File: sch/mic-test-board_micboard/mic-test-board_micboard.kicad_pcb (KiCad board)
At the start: 2 copper layers, 25 x 25 mm, 25 parts, among them J1 Conn_01x01, J2 Conn_01x01, J3 Conn_01x01, J4 Conn_01x01, J5 Conn_01x01, J6 Conn_01x04, U1 ICS-40730, U2 THS4531AIRUNR

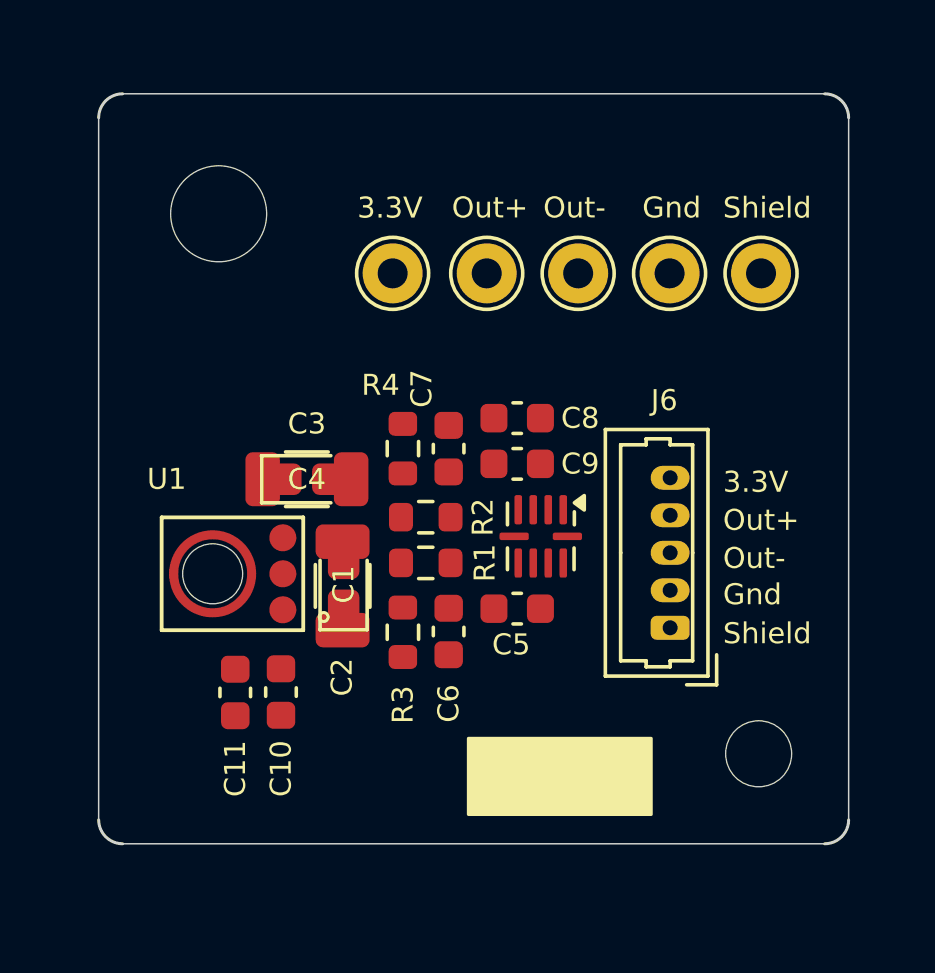
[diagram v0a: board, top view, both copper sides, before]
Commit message: pcb: finished routing mic board and ADC board.
 - BOM complete
 - uController pinout configured with CubeMX and re-checked
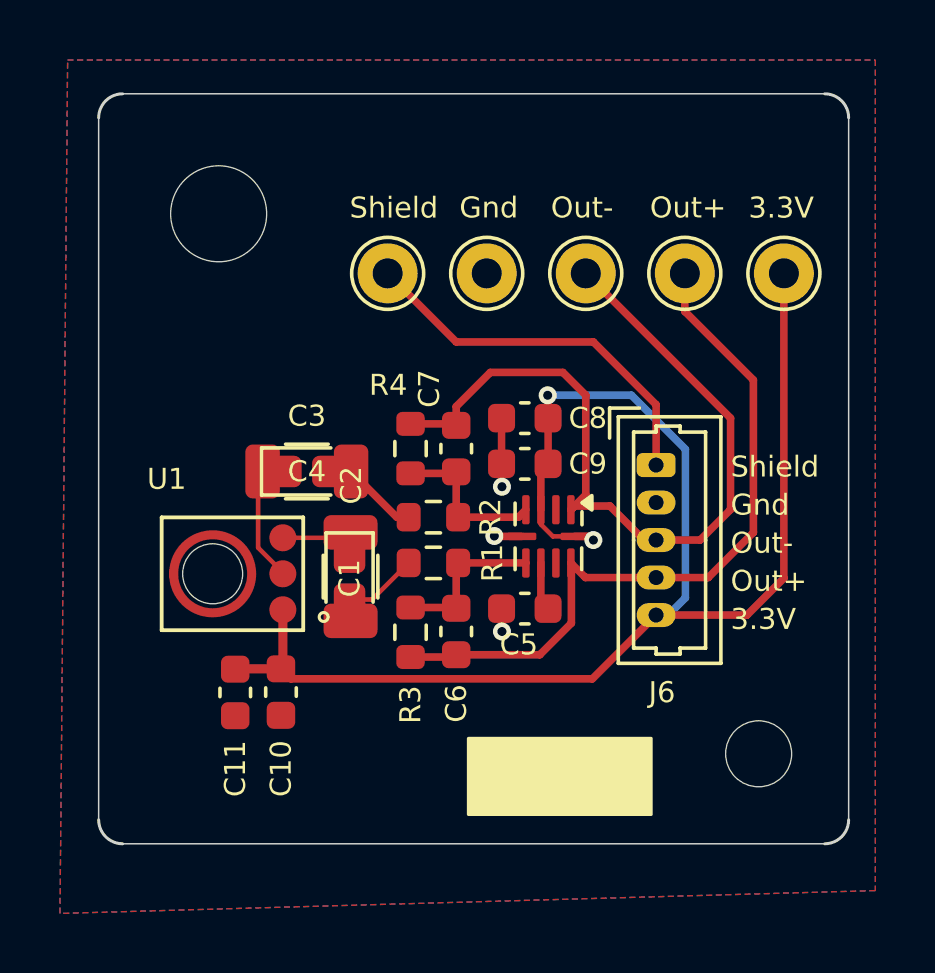
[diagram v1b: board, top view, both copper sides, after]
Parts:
- moved J1 13.0 mm to (150.9, 83.8)
- moved J5 12.4 mm to (137.7, 83.8)
- moved J2 6.60 mm to (147.6, 83.8)
- moved J4 6.10 mm to (141.0, 83.8)
- moved J6 5.44 mm to (146.6, 90.2), turned to -90 degrees
- moved C2 0.41 mm to (136.4, 93.9), turned to -90 degrees
- moved C1 0.29 mm to (136.4, 94.0), turned to -90 degrees
- moved C3 0.26 mm to (135.0, 90.4)
- moved C4 0.26 mm to (135.0, 90.4)
- moved C5 0.25 mm to (142.2, 95.0)
- moved C6 0.25 mm to (140.0, 95.8)
- moved C7 0.25 mm to (140.0, 89.7)
- moved C8 0.25 mm to (142.2, 88.6)
- moved C9 0.25 mm to (142.2, 90.2)
- moved R1 0.25 mm to (139.2, 93.5)
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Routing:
- net +3.3VA: track 0.00 -> 49.9 mm, vias 0 -> 2
- net Net-(J3-Pin_1): track 0.00 -> 27.4 mm
- net Net-(J2-Pin_1): track 0.00 -> 24.3 mm
- net /Shield: track 0.00 -> 12.8 mm
- net Net-(U2A-Vin+): track 0.00 -> 5.44 mm
- net Net-(U2A-VIn-): track 0.00 -> 5.33 mm
- net Net-(U1-OUTPUT-): track 0.00 -> 4.58 mm
- net GND: track 0.00 -> 3.98 mm, vias 0 -> 3
- net Net-(C3-Pad2): track 0.00 -> 3.31 mm
- net Net-(C1-Pad2): track 0.00 -> 3.20 mm
- net Net-(U1-OUTPUT+): track 0.00 -> 3.16 mm
- net /V_{OCM}: track 0.00 -> 1.62 mm
- added copper zone on B.Cu, net GND
- added copper zone on F.Cu, net GND

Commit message: pcb: ordered PCB's and BOM! RevA and v240506
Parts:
- J6: value Conn_01x04 -> Conn_01x05
- R1, R2: value 550R -> 549R
- R3, R4: value 1.6k -> 1.58k
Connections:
- U2 pad 2: (no net) -> unconnected-(U2A-NC-Pad2)
- U2 pad 8: (no net) -> unconnected-(U2A-NC-Pad8)
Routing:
- net +3.3VA: track 49.9 -> 51.1 mm, vias 2 -> 1
- net /Shield: track 12.8 -> 12.2 mm
- net GND: vias 3 -> 4
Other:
- board text added: "JBRRY SoundCompass Mic Test Board v20240506"
